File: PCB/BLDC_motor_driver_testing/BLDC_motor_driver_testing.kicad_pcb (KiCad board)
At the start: 4 copper layers, 90 x 63 mm, 78 parts, among them J1 PWR, J2 PHASE A, J3 PHASE B, J4 PHASE C, Q1 IRF540N, Q2 IRF540N, Q3 IRF540N, Q4 IRF540N, Q5 IRF540N, Q6 IRF540N, U1 AMS1117-3.3, U10 LMV393, U2 IR2104, U3 INA240A2D, U4 LMV393, U5 IR2104, U6 INA240A2D, U7 LMV393, U8 IR2104, U9 INA240A2D

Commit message: Getting closer to finish 2 ;)
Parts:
- moved J4 1.16 mm to (87.5, 77.0)
- moved J2 1.08 mm to (35.5, 77.0)
- moved J3 1.05 mm to (61.5, 77.0)
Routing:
- net +3.3V: track 61.8 -> 109.5 mm, vias 0 -> 18
- net ISENSE_A: track 4.05 -> 28.9 mm
- net PWM_IN_B: track 0.00 -> 21.9 mm
- net PWM_IN_A: track 0.00 -> 21.9 mm
- net PWM_IN_C: track 0.00 -> 21.9 mm
- net GND: track 61.7 -> 80.2 mm
- added copper zone on In1.Cu, net +3.3V

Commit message: Almost there 0_0
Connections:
- J2 pad 2: GND -> SD_A
- J3 pad 2: GND -> SD_B
- J4 pad 2: GND -> SD_C
- R13 pad 1: GND -> SD_B
- R19 pad 1: GND -> SD_C
- R7 pad 1: GND -> SD_A
- U10 pad 1: GND -> SD_C
- U2 pad 3: GND -> SD_A
- U4 pad 1: GND -> SD_A
- U5 pad 3: GND -> SD_B
- U7 pad 1: GND -> SD_B
- U8 pad 3: GND -> SD_C
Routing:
- net SD_C: track 0.00 -> 30.2 mm
- net SD_B: track 0.00 -> 30.2 mm
- net SD_A: track 0.00 -> 30.2 mm
- net ISENSE_C: track 4.05 -> 29.1 mm
- net ISENSE_B: track 4.05 -> 28.9 mm
- net GND: track 80.2 -> 58.3 mm
- net +3.3V: track 109.5 -> 90.6 mm, vias 18 -> 20
- net +5V: track 0.00 -> 11.3 mm
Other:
- board text added: "PWM SD ISENSE"

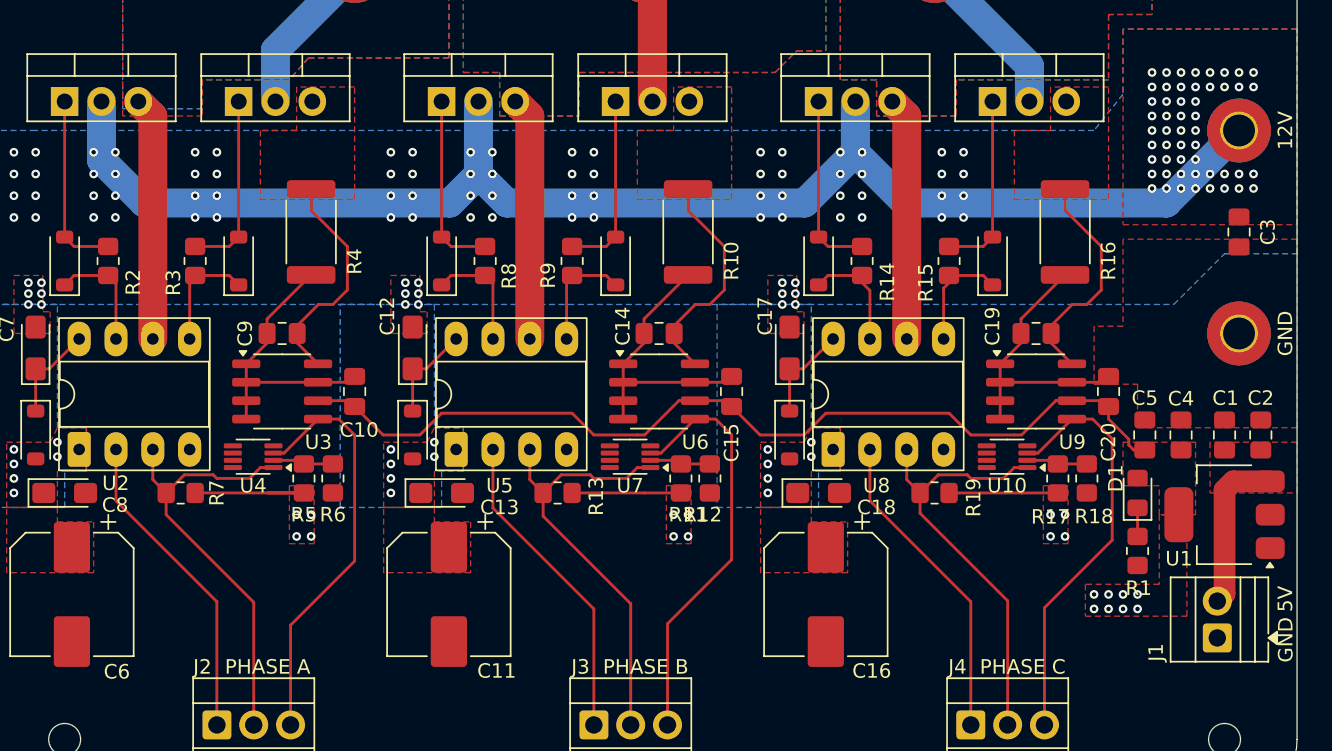
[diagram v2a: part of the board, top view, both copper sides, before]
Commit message: Gnd pours required, signal line EMI checking
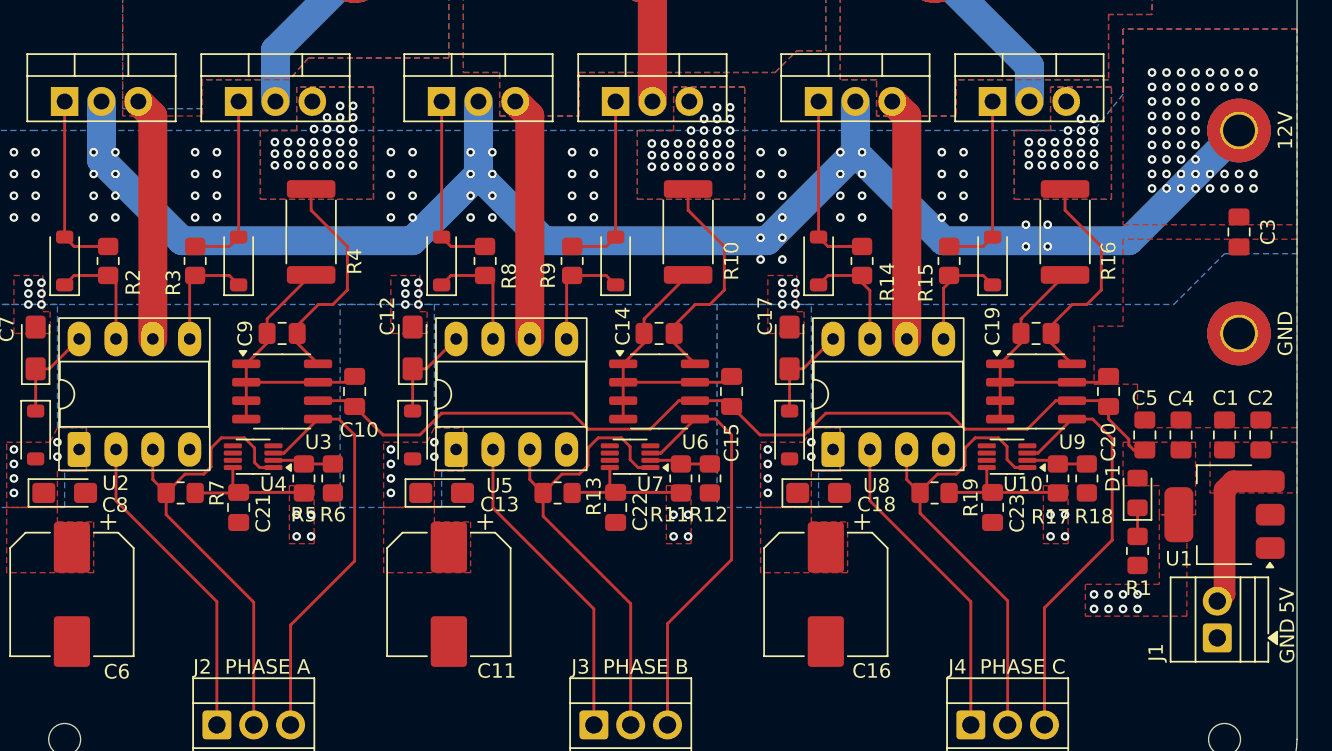
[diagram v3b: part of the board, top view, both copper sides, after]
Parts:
- added C21: 100n, Capacitor_SMD:C_0805_2012Metric_Pad1.18x1.45mm_HandSolder, F.Cu at (37.0, 62.0)
- added C22: 100n, Capacitor_SMD:C_0805_2012Metric_Pad1.18x1.45mm_HandSolder, F.Cu at (63.0, 62.0)
- added C23: 100n, Capacitor_SMD:C_0805_2012Metric_Pad1.18x1.45mm_HandSolder, F.Cu at (89.0, 62.0)
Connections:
- U10 pad 4: (no net) -> GND
- U10 pad 5: (no net) -> unconnected-(U10B-+-Pad5)
- U10 pad 6: (no net) -> unconnected-(U10B---Pad6)
- U10 pad 7: (no net) -> unconnected-(U10-Pad7)
- U10 pad 8: (no net) -> +3.3V
- U4 pad 4: (no net) -> GND
- U4 pad 5: (no net) -> unconnected-(U4B-+-Pad5)
- U4 pad 6: (no net) -> unconnected-(U4B---Pad6)
- U4 pad 7: (no net) -> unconnected-(U4-Pad7)
- U4 pad 8: (no net) -> +3.3V
- U7 pad 4: (no net) -> GND
- U7 pad 5: (no net) -> unconnected-(U7B-+-Pad5)
- U7 pad 6: (no net) -> unconnected-(U7B---Pad6)
- U7 pad 7: (no net) -> unconnected-(U7-Pad7)
- U7 pad 8: (no net) -> +3.3V
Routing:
- net +12V: track 98.9 -> 105.4 mm, vias 142 -> 150
- net SD_A: track 30.2 -> 33.1 mm
- net SD_C: track 30.2 -> 33.0 mm
- net SD_B: track 30.2 -> 32.9 mm
- net +3.3V: track 90.6 -> 93.1 mm
- net /BLDC driver phase C/GND_C: vias 0 -> 23
- net /BLDC driver phase B/GND_B: vias 0 -> 30
- net /BLDC driver phase A/GND_A: vias 0 -> 30
- added copper zone on B.Cu, net /BLDC driver phase A/GND_A
- added copper zone on In1.Cu, net /BLDC driver phase A/GND_A
- added copper zone on In2.Cu, net /BLDC driver phase A/GND_A
- added copper zone on B.Cu, net /BLDC driver phase B/GND_B
- added copper zone on In1.Cu, net /BLDC driver phase B/GND_B
- added copper zone on In2.Cu, net /BLDC driver phase B/GND_B
- added copper zone on B.Cu, net /BLDC driver phase C/GND_C
- added copper zone on In1.Cu, net /BLDC driver phase C/GND_C
- added copper zone on In2.Cu, net /BLDC driver phase C/GND_C

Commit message: Test driver layour finished... final touches
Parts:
- moved C14 4.00 mm to (70.0, 50.0)
- moved C19 4.00 mm to (96.0, 50.0)
- moved C9 4.00 mm to (44.0, 50.0)
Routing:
- net +12V: track 105.4 -> 316.0 mm, vias 150 -> 126
- net GND: track 58.3 -> 46.0 mm, vias 0 -> 126
- net +3.3V: track 93.1 -> 100.3 mm, vias 20 -> 22
- net Net-(D9-A): track 12.6 -> 14.5 mm
- net Net-(D6-A): track 12.6 -> 14.5 mm
- net Net-(D4-A): track 12.6 -> 14.5 mm
- net Net-(D3-A): track 12.6 -> 14.5 mm
- net Net-(D10-A): track 12.6 -> 14.5 mm
- net Net-(D7-A): track 12.6 -> 14.5 mm
- net /BLDC driver phase B/GND_B: track 15.7 -> 16.5 mm
- net /BLDC driver phase C/GND_C: track 15.7 -> 16.5 mm
- net /BLDC driver phase A/GND_A: track 15.7 -> 16.4 mm
- added copper zone on B.Cu, net GND
- added copper zone on In1.Cu, net GND
- added copper zone on In2.Cu, net GND

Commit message: more changes
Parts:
- C12, C17, C7: value 2.2u -> 22u
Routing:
- net GND: vias 126 -> 121
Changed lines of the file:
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@@
 			(plot_on_all_layers_selection 0x00000000_00000000_00000000_00000000)
 			(disableapertmacros no)
-			(usegerberextensions no)
-			(usegerberattributes yes)
-			(usegerberadvancedattributes yes)
-			(creategerberjobfile yes)
+			(usegerberextensions yes)
+			(usegerberattributes no)
+			(usegerberadvancedattributes no)
+			(creategerberjobfile no)
 			(dashed_line_dash_ratio 12.000000)
 			(dashed_line_gap_ratio 3.000000)
@@
 			(sketchdnponfab yes)
 			(crossoutdnponfab yes)
-			(subtractmaskfromsilk no)
+			(subtractmaskfromsilk yes)
 			(outputformat 1)
 			(mirror no)
-			(drillshape 1)
+			(drillshape 0)
 			(scaleselection 1)
-			(outputdirectory "")
+			(outputdirectory "BLDC_motor_driver_testing_gerber/")
 		)
 	)
@@
 			)
 		)
-		(property "Value" "2.2u"
+		(property "Value" "22u"
 			(at -1.013547 -1.853388 90)
 			(layer "F.Fab")
@@
 			)
 		)
-		(property "Value" "2.2u"
+		(property "Value" "22u"
 			(at -1.19 -2 90)
 			(layer "F.Fab")
@@
 			)
 		)
-		(property "Value" "2.2u"
+		(property "Value" "22u"
 			(at -0.932424 -1.734106 90)
 			(layer "F.Fab")
@@
 	)
 	(via
-		(at 101 52.8)
-		(size 0.6)
-		(drill 0.3)
-		(layers "F.Cu" "B.Cu")
-		(free yes)
-		(net 3)
-	)
-	(via
 		(at 105.4 46.9)
 		(size 0.6)
@@
 	)
 	(via
-		(at 103 52.8)
-		(size 0.6)
-		(drill 0.3)
-		(layers "F.Cu" "B.Cu")
-		(free yes)
-		(net 3)
-	)
-	(via
 		(at 43.5 62.3)
 		(size 0.6)
@@
 	)
 	(via
-		(at 100 52.8)
-		(size 0.6)
-		(drill 0.3)
-		(layers "F.Cu" "B.Cu")
-		(free yes)
-		(net 3)
-	)
-	(via
 		(at 100 50.8)
 		(size 0.6)
@@
 	)
 	(via
-		(at 99 52.8)
-		(size 0.6)
-		(drill 0.3)
-		(layers "F.Cu" "B.Cu")
-		(free yes)
-		(net 3)
-	)
-	(via
 		(at 92.1 49.6)
 		(size 0.6)
@@
 		(size 0.6)
 		(drill 0.3)
-		(layers "F.Cu" "B.Cu")
-		(free yes)
-		(net 3)
-	)
-	(via
-		(at 102 52.8)
-		(size 0.6)
-		(drill 0.3)

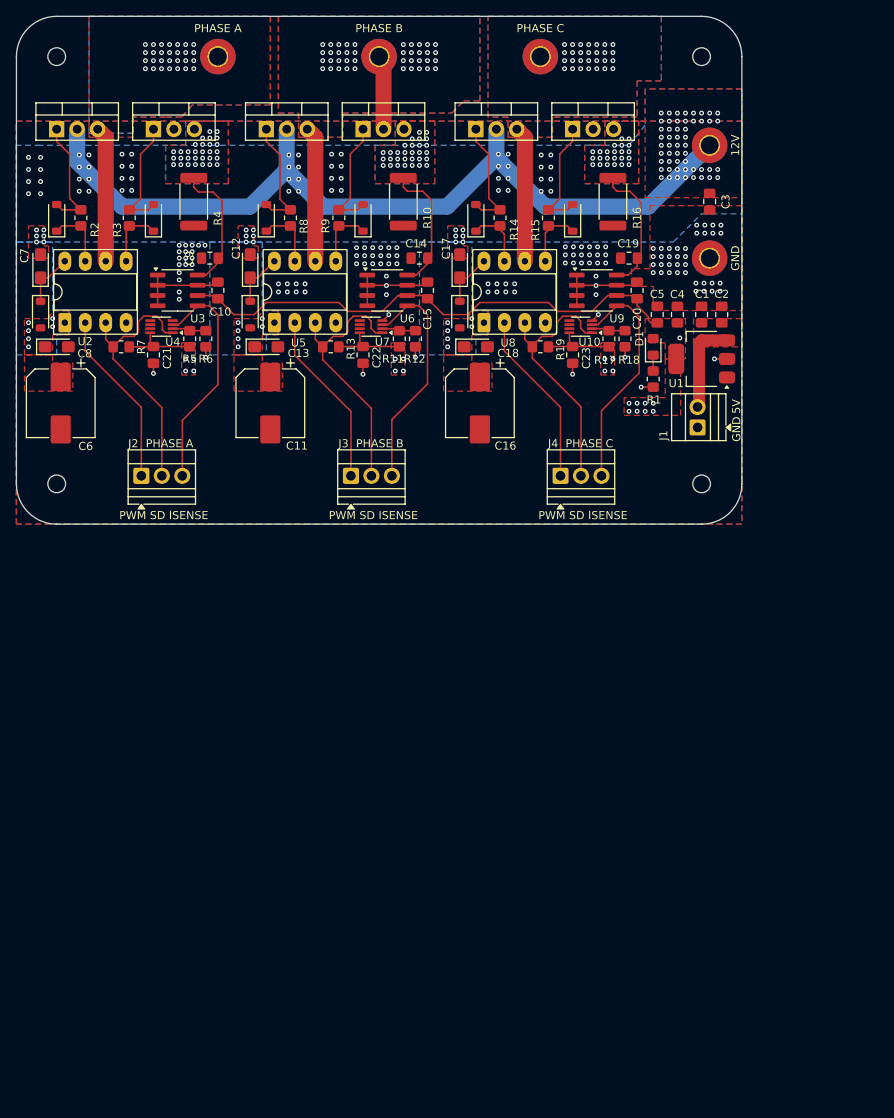
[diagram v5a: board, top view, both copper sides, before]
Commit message: small corrections for test driver
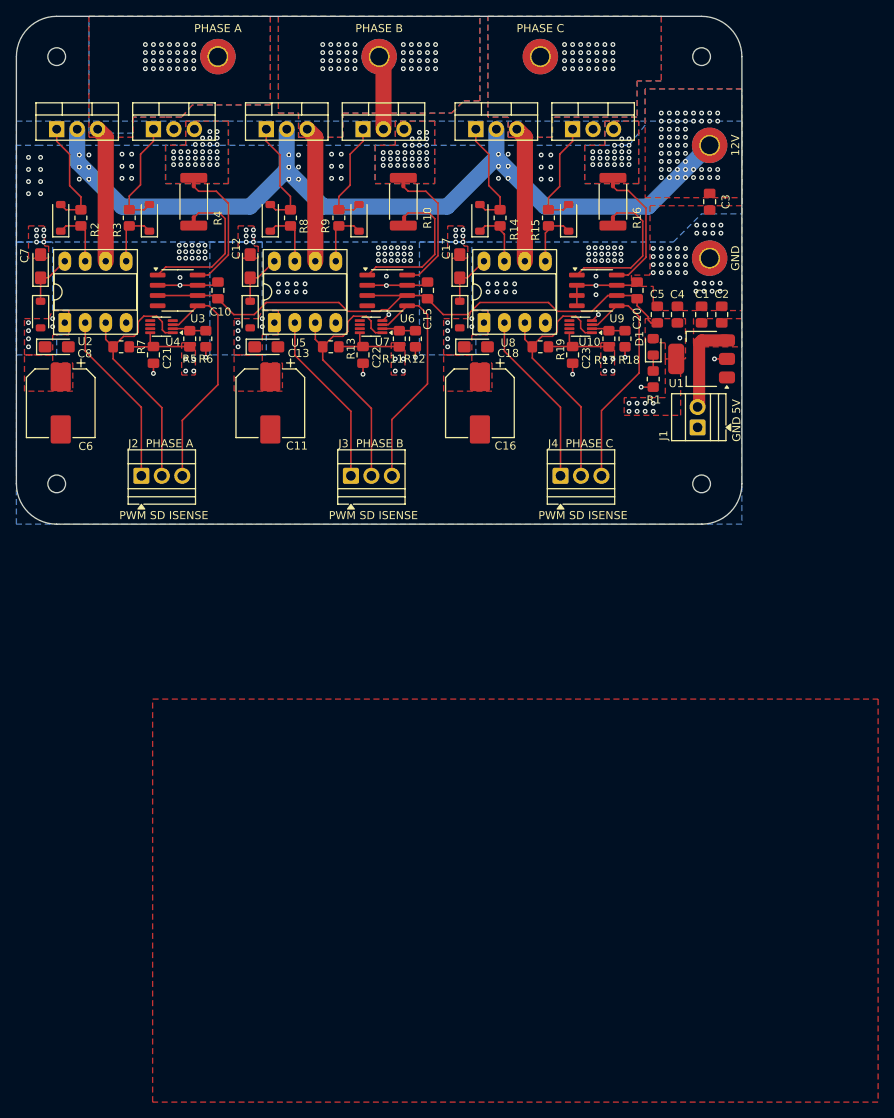
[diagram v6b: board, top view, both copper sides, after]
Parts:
- removed C14, C19, C9: 100n, Capacitor_SMD:C_0805_2012Metric_Pad1.18x1.45mm_HandSolder
- added NT1: NetTie_2, NetTie:NetTie-2_SMD_Pad0.5mm, F.Cu at (42.0, 45.4)
- added NT2: NetTie_2, NetTie:NetTie-2_SMD_Pad0.5mm, F.Cu at (42.0, 40.6)
- added NT3: NetTie_2, NetTie:NetTie-2_SMD_Pad0.5mm, F.Cu at (68.1, 45.4)
- added NT4: NetTie_2, NetTie:NetTie-2_SMD_Pad0.5mm, F.Cu at (68.0, 40.6)
- added NT5: NetTie_2, NetTie:NetTie-2_SMD_Pad0.5mm, F.Cu at (94.0, 40.6)
- added NT6: NetTie_2, NetTie:NetTie-2_SMD_Pad0.5mm, F.Cu at (94.0, 45.4)
- R4: value 1mR -> 2mR
- moved D10 0.50 mm to (88.5, 45.0)
- moved D3 0.50 mm to (25.5, 45.0)
- moved D4 0.50 mm to (36.5, 45.0)
- moved D6 0.50 mm to (51.5, 45.0)
- moved D7 0.50 mm to (62.5, 45.0)
- moved D9 0.50 mm to (77.5, 45.0)
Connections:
- U3 pad 1: GND -> /BLDC driver phase A/N_CURR_A
- U3 pad 3: GND -> +3.3V
- U3 pad 8: /BLDC driver phase A/GND_A -> /BLDC driver phase A/P_CURR_A
- U6 pad 1: GND -> /BLDC driver phase B/N_CURR_B
- U6 pad 3: GND -> +3.3V
- U6 pad 8: /BLDC driver phase B/GND_B -> /BLDC driver phase B/P_CURR_B
- U9 pad 1: GND -> /BLDC driver phase C/N_CURR_C
- U9 pad 3: GND -> +3.3V
- U9 pad 8: /BLDC driver phase C/GND_C -> /BLDC driver phase C/P_CURR_C
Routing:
- net /BLDC driver phase A/N_CURR_A: track 0.00 -> 18.2 mm
- net /BLDC driver phase B/N_CURR_B: track 0.00 -> 18.2 mm
- net /BLDC driver phase C/N_CURR_C: track 0.00 -> 17.8 mm
- net /BLDC driver phase B/GND_B: track 16.5 -> 0.00 mm
- net /BLDC driver phase C/GND_C: track 16.5 -> 0.00 mm
- net /BLDC driver phase B/P_CURR_B: track 0.00 -> 16.5 mm
- net /BLDC driver phase A/P_CURR_A: track 0.00 -> 16.4 mm
- net /BLDC driver phase A/GND_A: track 16.4 -> 0.46 mm
- net /BLDC driver phase C/P_CURR_C: track 0.00 -> 15.9 mm
- net +3.3V: track 100.3 -> 110.2 mm
- net GND: track 46.0 -> 37.4 mm, vias 121 -> 119
- net Net-(D9-K): track 7.87 -> 7.37 mm
- net Net-(D9-A): track 14.5 -> 14.0 mm
- net Net-(D7-K): track 7.81 -> 7.31 mm
- net Net-(D6-K): track 7.87 -> 7.37 mm
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
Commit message: getting there...
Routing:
- net +3.3V: track 110.2 -> 115.2 mm
- net GND: track 37.4 -> 34.9 mm, vias 119 -> 118

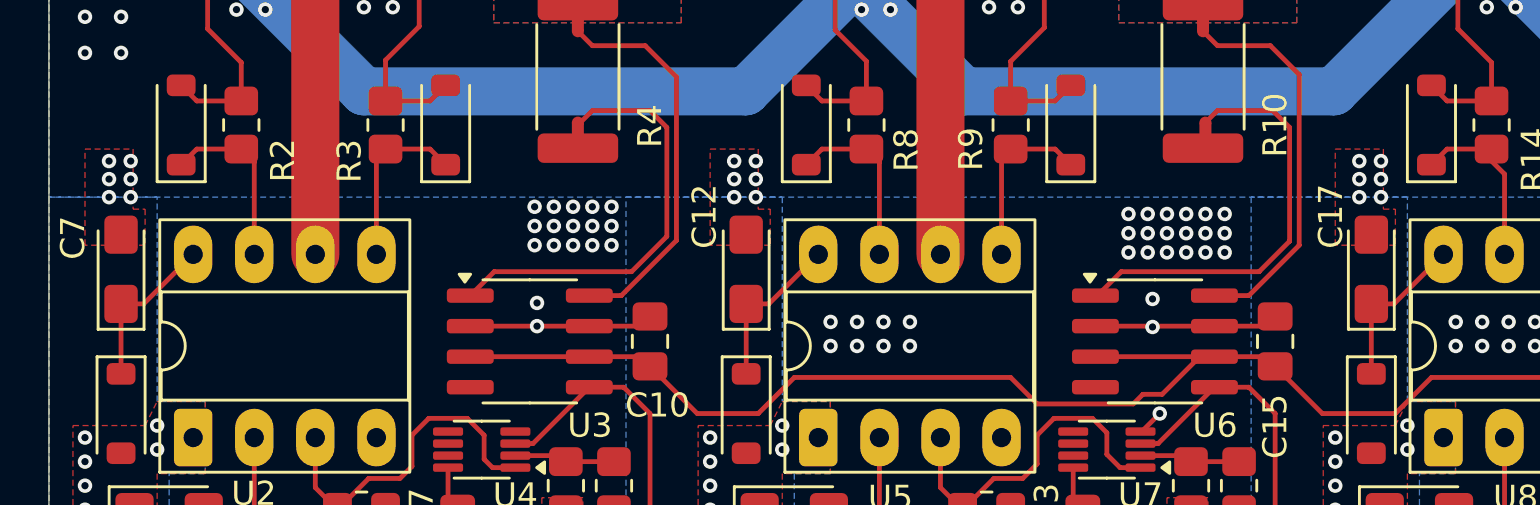
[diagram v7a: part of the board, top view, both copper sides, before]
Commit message: selected bootstrap caps and shunt resistor and csa gain
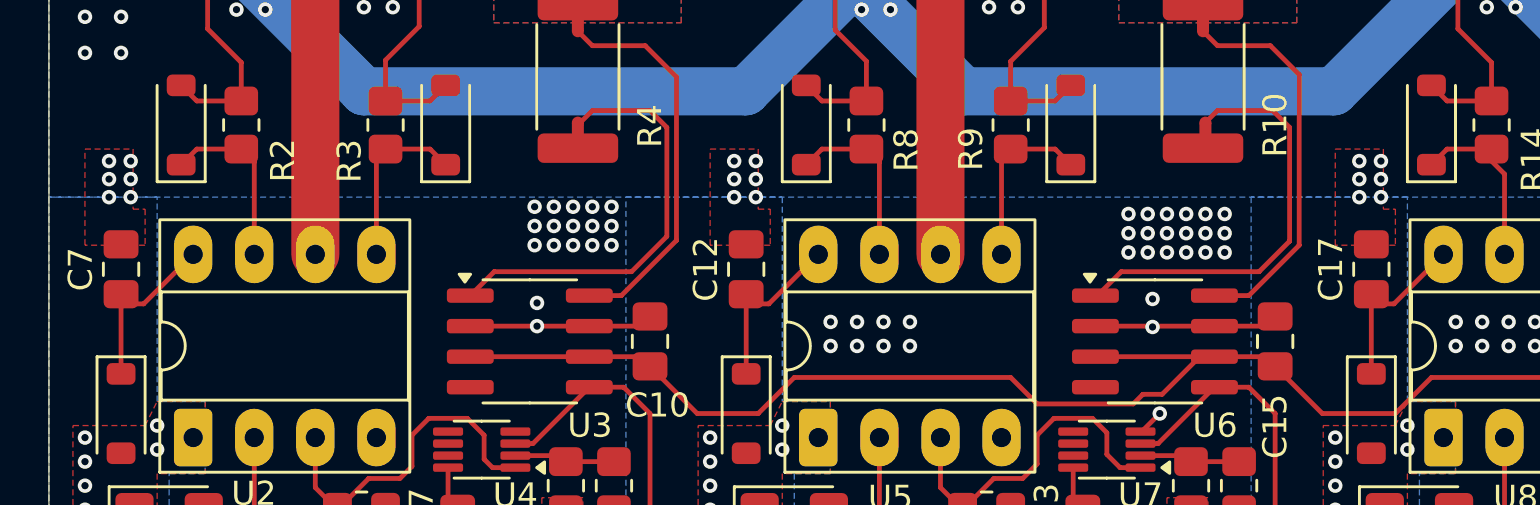
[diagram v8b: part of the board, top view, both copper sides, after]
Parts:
- C12, C17, C7: value 22u -> 2.2u; footprint Capacitor_Tantalum_SMD:CP_EIA-3216-18_Kemet-A_HandSolder -> Capacitor_SMD:C_0805_2012Metric_Pad1.18x1.45mm_HandSolder
- R10, R16: value 1mR -> 1.2mR
- R11, R17, R5: value 330R -> 1K
- R12, R18, R6: value 510R -> 10K
- R4: value 2mR -> 1.2mR
